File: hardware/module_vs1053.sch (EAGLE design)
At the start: 119 parts, among them IC1 IC_USBLC6-2, IC2 LM1117IMPX-3.3, IC3 PIC32MX795F512, IC4 DP83848, IC5 LM1117MPX-2.5, U1 USD-SOCKETUSD, U3 VS1053-L, X2 CRYSTALS-NOGND-CFPX-217, X3 KUSBVX, Y3 CRYSTAL-GROUNDEDSMD-5X3.2

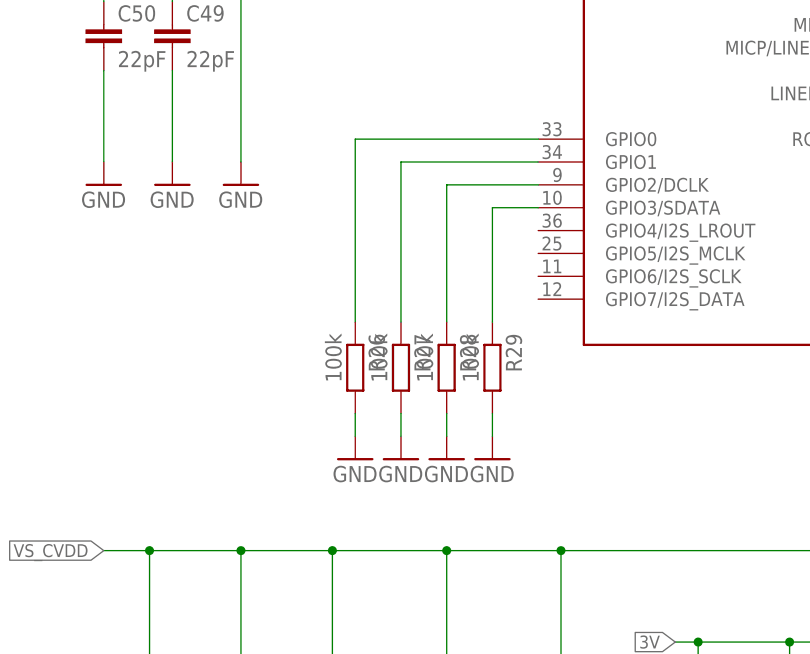
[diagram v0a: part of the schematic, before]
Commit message: VS1053 version updated
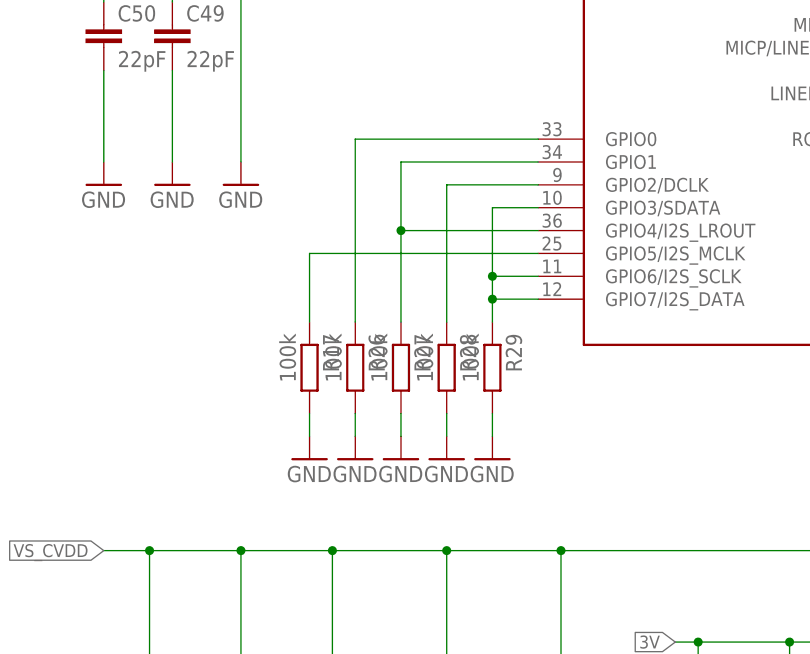
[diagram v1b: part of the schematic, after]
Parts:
- added R17: 100k, rcl:R-EU_R0402
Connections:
- new net N$2: R17.1, U3G$1.GPIO5/I2S_MCLK
- net GND: now also R17.2
- net VS_N$26: now also U3G$1.GPIO6/I2S_SCLK, U3G$1.GPIO7/I2S_DATA
- net VS_N$28: now also U3G$1.GPIO4/I2S_LROUT
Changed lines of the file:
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@@
 <part name="R16" library="rcl" deviceset="R-EU_" device="R0603"/>
 <part name="U3" library="vlsi-web" deviceset="VS1053" device="-L"/>
+<part name="R17" library="rcl" deviceset="R-EU_" device="R0402" value="100k"/>
+<part name="GND35" library="supply1" deviceset="GND" device=""/>
 </parts>
 <sheets>
@@
 <instance part="U3" gate="G$1" x="485.14" y="165.1"/>
 <instance part="U3" gate="P" x="622.3" y="88.9"/>
+<instance part="R17" gate="G$1" x="439.42" y="109.22" rot="R270"/>
+<instance part="GND35" gate="1" x="439.42" y="99.06"/>
 </instances>
 <busses>
@@
 <pinref part="GND3" gate="1" pin="GND"/>
 <wire x1="0" y1="538.48" x2="0" y2="541.02" width="0.1524" layer="91"/>
+</segment>
+<segment>
+<pinref part="R17" gate="G$1" pin="2"/>
+<pinref part="GND35" gate="1" pin="GND"/>
+<wire x1="439.42" y1="101.6" x2="439.42" y2="104.14" width="0.1524" layer="91"/>
 </segment>
 </net>
@@
 <pinref part="U3" gate="G$1" pin="GPIO3/SDATA"/>
 <wire x1="464.82" y1="127" x2="459.74" y2="127" width="0.1524" layer="91"/>
-<wire x1="459.74" y1="127" x2="459.74" y2="114.3" width="0.1524" layer="91"/>
+<wire x1="459.74" y1="127" x2="459.74" y2="119.38" width="0.1524" layer="91"/>
+<pinref part="U3" gate="G$1" pin="GPIO6/I2S_SCLK"/>
+<wire x1="459.74" y1="119.38" x2="459.74" y2="116.84" width="0.1524" layer="91"/>
+<wire x1="459.74" y1="116.84" x2="459.74" y2="114.3" width="0.1524" layer="91"/>
+<wire x1="464.82" y1="119.38" x2="459.74" y2="119.38" width="0.1524" layer="91"/>
+<junction x="459.74" y="119.38"/>
+<pinref part="U3" gate="G$1" pin="GPIO7/I2S_DATA"/>
+<wire x1="464.82" y1="116.84" x2="459.74" y2="116.84" width="0.1524" layer="91"/>
+<junction x="459.74" y="116.84"/>
 </segment>
 </net>
@@
 <pinref part="U3" gate="G$1" pin="GPIO1"/>
 <wire x1="464.82" y1="132.08" x2="449.58" y2="132.08" width="0.1524" layer="91"/>
-<wire x1="449.58" y1="132.08" x2="449.58" y2="114.3" width="0.1524" layer="91"/>
+<wire x1="449.58" y1="132.08" x2="449.58" y2="124.46" width="0.1524" layer="91"/>
+<pinref part="U3" gate="G$1" pin="GPIO4/I2S_LROUT"/>
+<wire x1="449.58" y1="124.46" x2="449.58" y2="114.3" width="0.1524" layer="91"/>
+<wire x1="464.82" y1="124.46" x2="449.58" y2="124.46" width="0.1524" layer="91"/>
+<junction x="449.58" y="124.46"/>
 </segment>
 </net>
@@
 </segment>
 </net>
+<net name="N$2" class="0">
+<segment>
+<pinref part="U3" gate="G$1" pin="GPIO5/I2S_MCLK"/>
+<pinref part="R17" gate="G$1" pin="1"/>
+<wire x1="464.82" y1="121.92" x2="439.42" y2="121.92" width="0.1524" layer="91"/>
+<wire x1="439.42" y1="121.92" x2="439.42" y2="114.3" width="0.1524" layer="91"/>
+</segment>
+</net>

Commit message: PCB updated
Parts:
- removed JP1: (no value), SparkFun-Connectors:AUDIO-JACKAUDIO_JACK2
- added J1: AUDIO_JACK_TRRSSMD_RA, SparkFun-Connectors:AUDIO_JACK_TRRSSMD_RA
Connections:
- net VS_AGND: now also J1.EARTH; no longer JP1.SLEEVE
- net VS_N$37: now also J1.RING1; no longer JP1.RIGHT
- net VS_N$38: now also J1.TIP; no longer JP1.LEFT
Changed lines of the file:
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@@
 <part name="C37" library="rcl" deviceset="C-EU" device="C0603" value="10n"/>
 <part name="C39" library="rcl" deviceset="C-EU" device="C0603" value="10n"/>
-<part name="JP1" library="SparkFun-Connectors" deviceset="AUDIO-JACK" device="AUDIO_JACK2"/>
 <part name="R26" library="rcl" deviceset="R-EU_" device="R0402" value="100k"/>
 <part name="R27" library="rcl" deviceset="R-EU_" device="R0402" value="100k"/>
@@
 <part name="R17" library="rcl" deviceset="R-EU_" device="R0402" value="100k"/>
 <part name="GND35" library="supply1" deviceset="GND" device=""/>
+<part name="J1" library="SparkFun-Connectors" deviceset="AUDIO_JACK_TRRS" device="SMD_RA"/>
 </parts>
 <sheets>
@@
 <instance part="C37" gate="G$1" x="538.48" y="127" rot="R180"/>
 <instance part="C39" gate="G$1" x="543.56" y="127" rot="R180"/>
-<instance part="JP1" gate="G$1" x="594.36" y="152.4" rot="R180"/>
 <instance part="R26" gate="G$1" x="444.5" y="109.22" rot="R270"/>
 <instance part="R27" gate="G$1" x="449.58" y="109.22" rot="R270"/>
@@
 <instance part="R17" gate="G$1" x="439.42" y="109.22" rot="R270"/>
 <instance part="GND35" gate="1" x="439.42" y="99.06"/>
+<instance part="J1" gate="G$1" x="617.22" y="154.94" rot="R180"/>
 </instances>
 <busses>
@@
 </segment>
 <segment>
-<pinref part="JP1" gate="G$1" pin="SLEEVE"/>
-<wire x1="589.28" y1="149.86" x2="584.2" y2="149.86" width="0.1524" layer="91"/>
-<wire x1="584.2" y1="149.86" x2="584.2" y2="137.16" width="0.1524" layer="91"/>
 <label x="584.2" y="134.62" size="1.4224" layer="95" rot="R270" xref="yes"/>
 <pinref part="R34" gate="G$1" pin="2"/>
@@
 <wire x1="571.5" y1="137.16" x2="571.5" y2="139.7" width="0.1524" layer="91"/>
 <junction x="576.58" y="137.16"/>
+<wire x1="584.2" y1="137.16" x2="604.52" y2="137.16" width="0.1524" layer="91"/>
+<wire x1="604.52" y1="137.16" x2="604.52" y2="149.86" width="0.1524" layer="91"/>
+<pinref part="J1" gate="G$1" pin="EARTH"/>
+<wire x1="604.52" y1="149.86" x2="612.14" y2="149.86" width="0.1524" layer="91"/>
 </segment>
 </net>
@@
 <pinref part="C44" gate="G$1" pin="2"/>
 <pinref part="R33" gate="G$1" pin="1"/>
-<wire x1="568.96" y1="152.4" x2="571.5" y2="152.4" width="0.1524" layer="91"/>
 <wire x1="571.5" y1="152.4" x2="571.5" y2="149.86" width="0.1524" layer="91"/>
-<pinref part="JP1" gate="G$1" pin="RIGHT"/>
-<wire x1="571.5" y1="152.4" x2="589.28" y2="152.4" width="0.1524" layer="91"/>
 <junction x="571.5" y="152.4"/>
+<wire x1="571.5" y1="152.4" x2="568.96" y2="152.4" width="0.1524" layer="91"/>
+<wire x1="571.5" y1="152.4" x2="612.14" y2="152.4" width="0.1524" layer="91"/>
+<pinref part="J1" gate="G$1" pin="RING1"/>
 </segment>
 </net>
@@
 <wire x1="568.96" y1="160.02" x2="576.58" y2="160.02" width="0.1524" layer="91"/>
 <wire x1="576.58" y1="160.02" x2="576.58" y2="149.86" width="0.1524" layer="91"/>
-<wire x1="576.58" y1="160.02" x2="584.2" y2="160.02" width="0.1524" layer="91"/>
-<wire x1="584.2" y1="160.02" x2="584.2" y2="154.94" width="0.1524" layer="91"/>
 <junction x="576.58" y="160.02"/>
-<pinref part="JP1" gate="G$1" pin="LEFT"/>
-<wire x1="584.2" y1="154.94" x2="589.28" y2="154.94" width="0.1524" layer="91"/>
-</segment>
-</net>
+<wire x1="576.58" y1="160.02" x2="604.52" y2="160.02" width="0.1524" layer="91"/>
+<pinref part="J1" gate="G$1" pin="TIP"/>
+<wire x1="612.14" y1="157.48" x2="604.52" y2="157.48" width="0.1524" layer="91"/>
+<wire x1="604.52" y1="157.48" x2="604.52" y2="160.02" width="0.1524" layer="91"/>
+</segment>
+</net>

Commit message: Changes in PCB design allowing us to use bug free I2C1 instead of buggy I2C3
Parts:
- removed R12: (no value), rcl:R-EU_R0603
- removed R14: (no value), rcl:R-EU_R0402
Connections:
- net 1WIRE renamed SCL1
- removed net LED: SV1.6
- removed net RA15_ROT_SW: IC3.RA15/INT4/SDA1/AETXEN
- removed net SCL1A: IC3.SCL1A/SDO1A/U1ATX/RF8, R12.1, SV1.1
- removed net SDA1A: IC3.SDA1A/SDI1A/U1ARX/RF2, R14.1, SV1.2
- new net RF2: IC3.SDA1A/SDI1A/U1ARX/RF2, SV1.2
- new net RF8: IC3.SCL1A/SDO1A/U1ATX/RF8, SV1.1
- new net SDA1: IC3.RA15/INT4/SDA1/AETXEN, SV1.6
- net 3V: no longer R12.2, R14.2
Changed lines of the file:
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@@
 <part name="C1" library="rcl" deviceset="C-EU" device="C0402"/>
 <part name="GND1" library="SparkFun-Aesthetics" deviceset="GND" device=""/>
-<part name="R12" library="rcl" deviceset="R-EU_" device="R0603"/>
-<part name="R14" library="rcl" deviceset="R-EU_" device="R0402"/>
 <part name="C2" library="rcl" deviceset="C-EU" device="C0402"/>
 <part name="GND3" library="SparkFun-Aesthetics" deviceset="GND" device=""/>
@@
 <instance part="C1" gate="G$1" x="22.86" y="546.1"/>
 <instance part="GND1" gate="1" x="22.86" y="535.94" rot="MR0"/>
-<instance part="R12" gate="G$1" x="144.78" y="393.7" rot="R90"/>
-<instance part="R14" gate="G$1" x="152.4" y="393.7" rot="R90"/>
 <instance part="C2" gate="G$1" x="0" y="546.1"/>
 <instance part="GND3" gate="1" x="0" y="535.94" rot="MR0"/>
@@
 </segment>
 <segment>
-<pinref part="R12" gate="G$1" pin="2"/>
-<wire x1="144.78" y1="398.78" x2="144.78" y2="401.32" width="0.1524" layer="91"/>
-<pinref part="R14" gate="G$1" pin="2"/>
-<wire x1="144.78" y1="401.32" x2="149.86" y2="401.32" width="0.1524" layer="91"/>
-<wire x1="149.86" y1="401.32" x2="152.4" y2="401.32" width="0.1524" layer="91"/>
-<wire x1="152.4" y1="401.32" x2="152.4" y2="398.78" width="0.1524" layer="91"/>
-<wire x1="149.86" y1="401.32" x2="149.86" y2="406.4" width="0.1524" layer="91"/>
-<junction x="149.86" y="401.32"/>
-<label x="149.86" y="406.4" size="1.4224" layer="95" rot="R90" xref="yes"/>
-</segment>
-<segment>
 <pinref part="L3" gate="L" pin="1"/>
 <wire x1="419.1" y1="-73.66" x2="419.1" y2="-68.58" width="0.1524" layer="91"/>
@@
 </segment>
 </net>
-<net name="1WIRE" class="0">
+<net name="SCL1" class="0">
 <segment>
 <pinref part="IC3" gate="G$1" pin="RA14/INT3/SCL1/AETXCLK"/>
@@
 <wire x1="340.36" y1="246.38" x2="345.44" y2="246.38" width="0.1524" layer="91"/>
 <label x="345.44" y="246.38" size="1.4224" layer="95" xref="yes"/>
-</segment>
-</net>
-<net name="LED" class="0">
-<segment>
-<pinref part="SV1" gate="G$1" pin="6"/>
-<wire x1="325.12" y1="248.92" x2="320.04" y2="248.92" width="0.1524" layer="91"/>
-<label x="320.04" y="248.92" size="1.4224" layer="95" rot="R180" xref="yes"/>
 </segment>
 </net>
@@
 </segment>
 </net>
-<net name="SCL1A" class="0">
+<net name="RF8" class="0">
 <segment>
 <pinref part="IC3" gate="G$1" pin="SCL1A/SDO1A/U1ATX/RF8"/>
-<wire x1="114.3" y1="368.3" x2="144.78" y2="368.3" width="0.1524" layer="91"/>
-<label x="154.94" y="368.3" size="1.4224" layer="95" xref="yes"/>
-<pinref part="R12" gate="G$1" pin="1"/>
-<wire x1="144.78" y1="368.3" x2="154.94" y2="368.3" width="0.1524" layer="91"/>
-<wire x1="144.78" y1="388.62" x2="144.78" y2="368.3" width="0.1524" layer="91"/>
-<junction x="144.78" y="368.3"/>
+<wire x1="114.3" y1="368.3" x2="119.38" y2="368.3" width="0.1524" layer="91"/>
+<label x="119.38" y="368.3" size="1.4224" layer="95" xref="yes"/>
 </segment>
 <segment>
@@
 </segment>
 </net>
-<net name="SDA1A" class="0">
+<net name="RF2" class="0">
 <segment>
 <pinref part="IC3" gate="G$1" pin="SDA1A/SDI1A/U1ARX/RF2"/>
-<wire x1="114.3" y1="383.54" x2="152.4" y2="383.54" width="0.1524" layer="91"/>
-<label x="154.94" y="383.54" size="1.4224" layer="95" xref="yes"/>
-<pinref part="R14" gate="G$1" pin="1"/>
-<wire x1="152.4" y1="383.54" x2="154.94" y2="383.54" width="0.1524" layer="91"/>
-<wire x1="152.4" y1="388.62" x2="152.4" y2="383.54" width="0.1524" layer="91"/>
-<junction x="152.4" y="383.54"/>
+<wire x1="114.3" y1="383.54" x2="119.38" y2="383.54" width="0.1524" layer="91"/>
+<label x="119.38" y="383.54" size="1.4224" layer="95" xref="yes"/>
 </segment>
 <segment>
@@
 </segment>
 </net>
-<net name="RA15_ROT_SW" class="0">
+<net name="SDA1" class="0">
 <segment>
 <pinref part="IC3" gate="G$1" pin="RA15/INT4/SDA1/AETXEN"/>
@@
 <label x="15.24" y="406.4" size="1.4224" layer="95" rot="R180" xref="yes"/>
 </segment>
-</net>
+<segment>
+<pinref part="SV1" gate="G$1" pin="6"/>
+<wire x1="325.12" y1="248.92" x2="320.04" y2="248.92" width="0.1524" layer="91"/>
+<label x="320.04" y="248.92" size="1.4224" layer="95" rot="R180" xref="yes"/>
+</segment>
+</net>

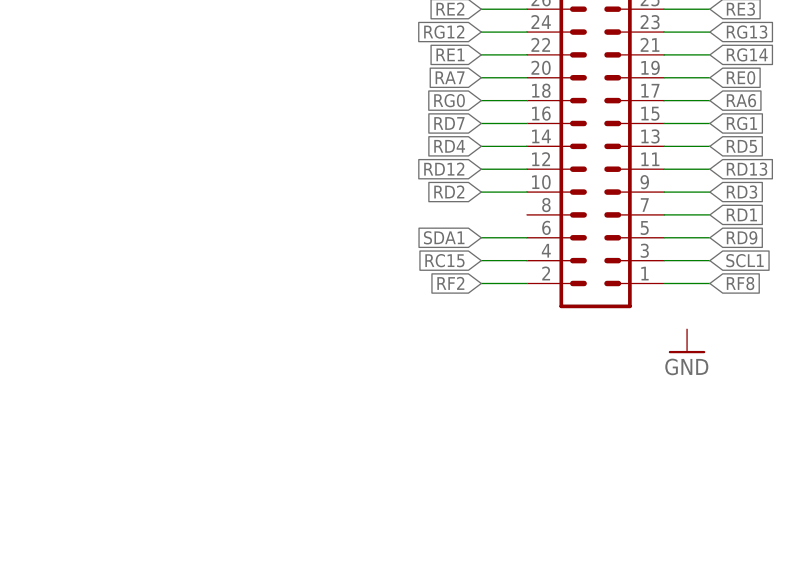
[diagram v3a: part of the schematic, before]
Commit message: Changes to prepare project for analog radio funcionality
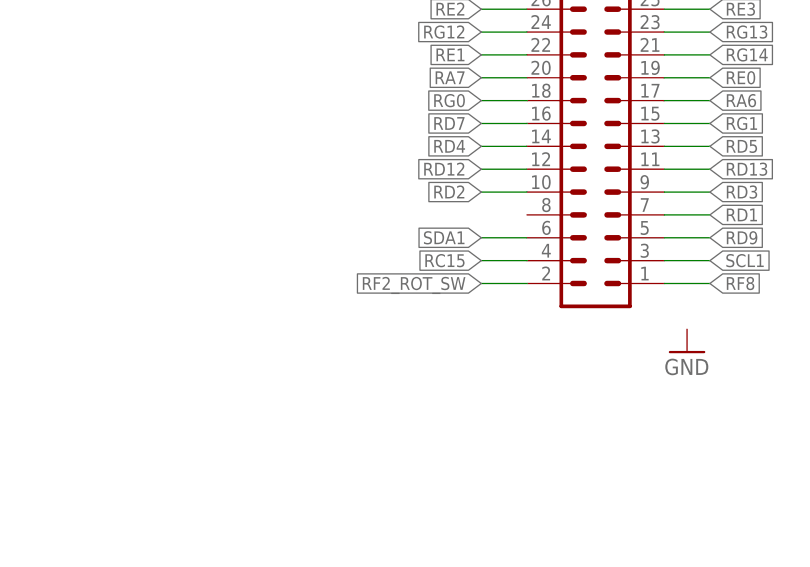
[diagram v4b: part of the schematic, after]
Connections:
- new net RF2_ROT_SW: SV1.2
- net RF2: no longer SV1.2
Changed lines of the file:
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@@
 <label x="119.38" y="383.54" size="1.4224" layer="95" xref="yes"/>
-</segment>
-<segment>
-<pinref part="SV1" gate="G$1" pin="2"/>
-<wire x1="325.12" y1="243.84" x2="320.04" y2="243.84" width="0.1524" layer="91"/>
-<label x="320.04" y="243.84" size="1.4224" layer="95" rot="R180" xref="yes"/>
 </segment>
 </net>
@@
 </segment>
 </net>
+<net name="RF2_ROT_SW" class="0">
+<segment>
+<pinref part="SV1" gate="G$1" pin="2"/>
+<wire x1="325.12" y1="243.84" x2="320.04" y2="243.84" width="0.1524" layer="91"/>
+<label x="320.04" y="243.84" size="1.4224" layer="95" rot="R180" xref="yes"/>
+</segment>
+</net>

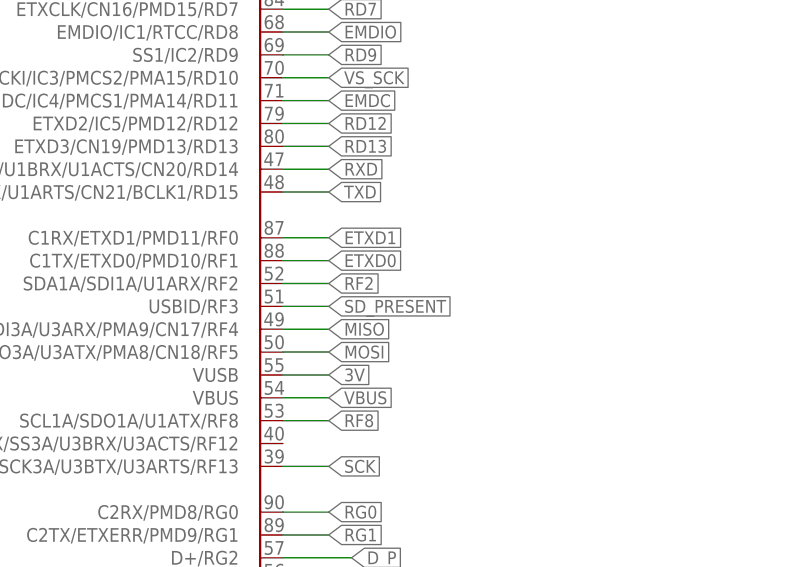
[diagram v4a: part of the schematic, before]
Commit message: PCB broken line fixed
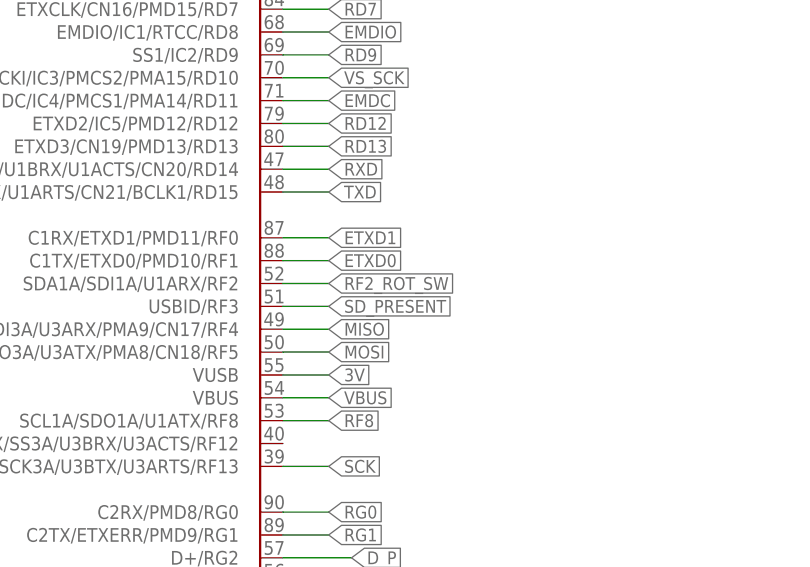
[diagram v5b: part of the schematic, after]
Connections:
- removed net RF2: IC3.SDA1A/SDI1A/U1ARX/RF2
- net RF2_ROT_SW: now also IC3.SDA1A/SDI1A/U1ARX/RF2
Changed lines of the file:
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@@
-</segment>
-</net>
-<net name="RF2" class="0">
-<segment>
-<pinref part="IC3" gate="G$1" pin="SDA1A/SDI1A/U1ARX/RF2"/>
-<wire x1="114.3" y1="383.54" x2="119.38" y2="383.54" width="0.1524" layer="91"/>
-<label x="119.38" y="383.54" size="1.4224" layer="95" xref="yes"/>
 </segment>
 </net>
@@
 <label x="320.04" y="243.84" size="1.4224" layer="95" rot="R180" xref="yes"/>
 </segment>
+<segment>
+<pinref part="IC3" gate="G$1" pin="SDA1A/SDI1A/U1ARX/RF2"/>
+<wire x1="114.3" y1="383.54" x2="119.38" y2="383.54" width="0.1524" layer="91"/>
+<label x="119.38" y="383.54" size="1.4224" layer="95" xref="yes"/>
+</segment>
 </net>
